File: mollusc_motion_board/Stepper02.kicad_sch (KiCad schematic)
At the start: 7 parts, among them J3 RJ45 x4, U6 74HC14, U6 SN74AHCT125N

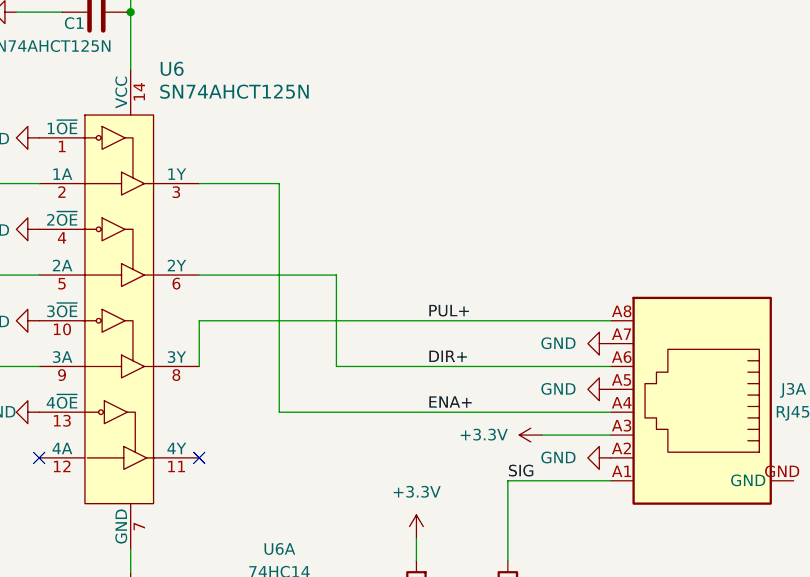
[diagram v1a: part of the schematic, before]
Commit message: adding ethernet jack
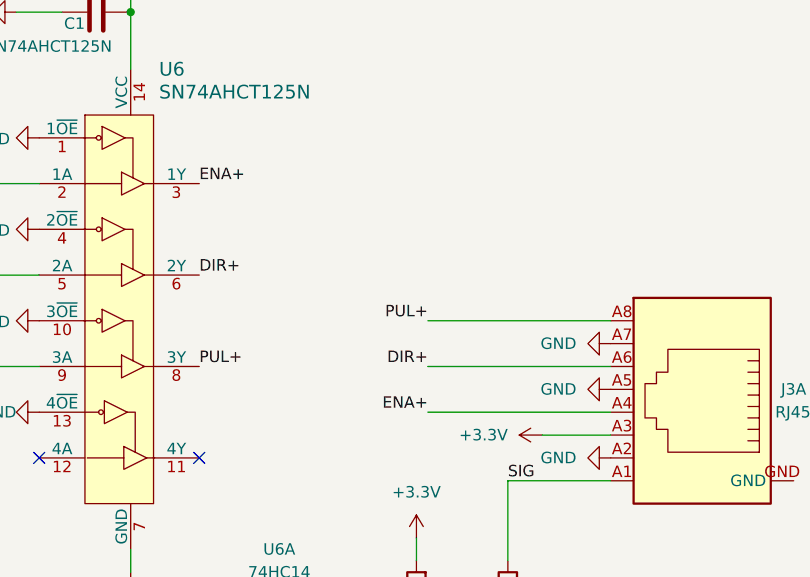
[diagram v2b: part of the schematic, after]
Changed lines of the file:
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@@
-    (stroke (width 0) (type default))
-  )
-  (wire (pts (xy 151.13 113.03) (xy 151.13 87.63))
     (stroke (width 0) (type default))
   )
@@
     (stroke (width 0) (type default))
   )
-  (wire (pts (xy 157.48 107.95) (xy 187.96 107.95))
-    (stroke (width 0) (type default))
-  )
-  (wire (pts (xy 142.24 102.87) (xy 142.24 107.95))
-    (stroke (width 0) (type default))
-  )
   (wire (pts (xy 176.53 120.65) (xy 187.96 120.65))
     (stroke (width 0) (type default))
   )
-  (wire (pts (xy 142.24 97.79) (xy 157.48 97.79))
+  (wire (pts (xy 167.64 113.03) (xy 187.96 113.03))
     (stroke (width 0) (type default))
   )
@@
     (stroke (width 0) (type default))
   )
-  (wire (pts (xy 157.48 97.79) (xy 157.48 107.95))
+  (wire (pts (xy 167.64 102.87) (xy 187.96 102.87))
     (stroke (width 0) (type default))
   )
@@
     (stroke (width 0) (type default))
   )
-  (wire (pts (xy 142.24 102.87) (xy 187.96 102.87))
-    (stroke (width 0) (type default))
-  )
   (wire (pts (xy 158.75 137.16) (xy 166.37 137.16))
     (stroke (width 0) (type default))
   )
-  (wire (pts (xy 134.62 128.27) (xy 134.62 130.81))
+  (wire (pts (xy 167.64 107.95) (xy 187.96 107.95))
     (stroke (width 0) (type default))
   )
-  (wire (pts (xy 151.13 113.03) (xy 187.96 113.03))
+  (wire (pts (xy 134.62 128.27) (xy 134.62 130.81))
     (stroke (width 0) (type default))
   )
@@
     (stroke (width 0) (type default))
   )
-  (wire (pts (xy 151.13 87.63) (xy 142.24 87.63))
-    (stroke (width 0) (type default))
-  )
   (wire (pts (xy 134.62 68.58) (xy 134.62 74.93))
     (stroke (width 0) (type default))
@@
     (effects (font (size 5.08 5.08)) (justify left bottom))
   )
-  (label "ENA+" (at 167.64 113.03 0) (fields_autoplaced)
+  (label "ENA+" (at 167.64 113.03 180) (fields_autoplaced)
+    (effects (font (size 1.27 1.27)) (justify right bottom))
+  )
+  (label "DIR+" (at 167.64 107.95 180) (fields_autoplaced)
+    (effects (font (size 1.27 1.27)) (justify right bottom))
+  )
+  (label "ENA+" (at 142.24 87.63 0) (fields_autoplaced)
     (effects (font (size 1.27 1.27)) (justify left bottom))
   )
-  (label "DIR+" (at 167.64 107.95 0) (fields_autoplaced)
+  (label "PUL+" (at 142.24 107.95 0) (fields_autoplaced)
     (effects (font (size 1.27 1.27)) (justify left bottom))
   )
@@
     (effects (font (size 1.27 1.27)) (justify left bottom))
   )
-  (label "PUL+" (at 167.64 102.87 0) (fields_autoplaced)
+  (label "DIR+" (at 142.24 97.79 0) (fields_autoplaced)
     (effects (font (size 1.27 1.27)) (justify left bottom))
   )
+  (label "PUL+" (at 167.64 102.87 180) (fields_autoplaced)
+    (effects (font (size 1.27 1.27)) (justify right bottom))
+  )
   (hierarchical_label "Stepper_ENABLE" (shape input) (at 114.3 87.63 180) (fields_autoplaced)

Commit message: Board v2 wip
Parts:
- C1, C3: value 0.1uF 16V -> 0.1uF 50V; footprint HangOn_Mainboard:R0603 -> molluscmotion:C0603
- R1, R2: footprint HangOn_Mainboard:R0603 -> molluscmotion:R0603
- U6: footprint HangOn_Mainboard:SOIC-14_L8.7-W3.9-P1.27-LS6.0-BL -> molluscmotion:SOIC-14_L8.7-W3.9-P1.27-LS6.0-BL
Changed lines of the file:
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@@
       (effects (font (size 1.27 1.27)) (justify left))
     )
-    (property "Value" "0.1uF 16V" (at 169.291 142.113 0)
-      (effects (font (size 1.27 1.27)) (justify left))
-    )
-    (property "Footprint" "HangOn_Mainboard:R0603" (at 167.3352 144.78 0)
+    (property "Value" "0.1uF 50V " (at 169.291 142.113 0)
+      (effects (font (size 1.27 1.27)) (justify left))
+    )
+    (property "Footprint" "molluscmotion:C0603" (at 167.3352 144.78 0)
       (effects (font (size 1.27 1.27)) hide)
     )
@@
       (effects (font (size 1.27 1.27)) (justify right))
     )
-    (property "Footprint" "HangOn_Mainboard:R0603" (at 168.148 133.35 90)
+    (property "Footprint" "molluscmotion:R0603" (at 168.148 133.35 90)
       (effects (font (size 1.27 1.27)) hide)
     )
@@
       (effects (font (size 1.27 1.27)))
     )
-    (property "Footprint" "HangOn_Mainboard:SOIC-14_L8.7-W3.9-P1.27-LS6.0-BL" (at 151.13 137.16 0)
+    (property "Footprint" "molluscmotion:SOIC-14_L8.7-W3.9-P1.27-LS6.0-BL" (at 151.13 137.16 0)
       (effects (font (size 1.27 1.27)) hide)
     )
@@
         )
         (path "/351cebb8-982f-46d7-8218-395788e5ce03/c416ce84-8678-4ab5-ab91-bfcc4d019431"
-          (reference "J4") (unit 2)
+          (reference "J4") (unit 3)
         )
       )
@@
       (effects (font (size 1.27 1.27)) (justify left))
     )
-    (property "Footprint" "HangOn_Mainboard:R0603" (at 174.752 133.35 90)
+    (property "Footprint" "molluscmotion:R0603" (at 174.752 133.35 90)
       (effects (font (size 1.27 1.27)) hide)
     )
@@
       (effects (font (size 1.524 1.524)) (justify left))
     )
-    (property "Footprint" "HangOn_Mainboard:SOIC-14_L8.7-W3.9-P1.27-LS6.0-BL" (at 139.7 87.63 0)
+    (property "Footprint" "molluscmotion:SOIC-14_L8.7-W3.9-P1.27-LS6.0-BL" (at 139.7 87.63 0)
       (effects (font (size 1.524 1.524)) (justify left) hide)
     )
@@
       (effects (font (size 1.27 1.27)) (justify left))
     )
-    (property "Value" "0.1uF 16V " (at 133.35 64.77 90)
-      (effects (font (size 1.27 1.27)) (justify left))
-    )
-    (property "Footprint" "HangOn_Mainboard:R0603" (at 134.62 67.6148 0)
-      (effects (font (size 1.27 1.27)) hide)
-    )
+    (property "Value" "0.1uF 50V " (at 133.35 64.77 90)
+      (effects (font (size 1.27 1.27)) (justify left))
+    )
+    (property "Footprint" "molluscmotion:C0603" (at 134.62 67.6148 0)
+      (effects (font (size 1.27 1.27)) hide)
+    )

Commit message: PCB v1.2 Layout
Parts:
- added D5: ESD5Z5_0T1G, molluscmotion:SOD-523F_L1.2-W0.8-LS1.7-RD, symbol molluscmotion:ESD5Z5_0T1G
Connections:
- net GND: now also D5.2 (A)
- net at C3.1, R1.1, R2.2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: now also D5.1 (C)
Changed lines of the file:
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@@
 (kicad_sch (version 20230121) (generator eeschema)
   (paper "A4")
+  (junction (at 171.45 148.59) (diameter 0) (color 0 0 0 0)
+  )
   (junction (at 166.37 137.16) (diameter 0) (color 0 0 0 0)
   )
   (junction (at 134.62 68.58) (diameter 0) (color 0 0 0 0)
+  )
+  (junction (at 176.53 137.16) (diameter 0) (color 0 0 0 0)
   )
   (no_connect (at 142.24 118.11))
@@
     (stroke (width 0) (type default))
   )
+  (wire (pts (xy 166.37 148.59) (xy 171.45 148.59))
+    (stroke (width 0) (type default))
+  )
+  (wire (pts (xy 176.53 147.32) (xy 176.53 148.59))
+    (stroke (width 0) (type default))
+  )
   (wire (pts (xy 114.3 97.79) (xy 124.46 97.79))
     (stroke (width 0) (type default))
@@
     (stroke (width 0) (type default))
   )
+  (wire (pts (xy 171.45 148.59) (xy 176.53 148.59))
+    (stroke (width 0) (type default))
+  )
   (wire (pts (xy 143.51 137.16) (xy 127 137.16))
     (stroke (width 0) (type default))
   )
-  (wire (pts (xy 166.37 147.32) (xy 166.37 144.78))
+  (wire (pts (xy 171.45 148.59) (xy 171.45 151.13))
     (stroke (width 0) (type default))
   )
   (wire (pts (xy 114.3 87.63) (xy 124.46 87.63))
+    (stroke (width 0) (type default))
+  )
+  (wire (pts (xy 166.37 144.78) (xy 166.37 148.59))
     (stroke (width 0) (type default))
   )
@@
   (symbol (lib_id "Device:C") (at 166.37 140.97 0) (unit 1)
     (in_bom yes) (on_board yes) (dnp no)
-    (property "Reference" "C3" (at 169.291 139.8016 0)
+    (property "Reference" "C3" (at 161.29 142.24 0)
       (effects (font (size 1.27 1.27)) (justify left))
     )
-    (property "Value" "0.1uF 50V " (at 169.291 142.113 0)
+    (property "Value" "0.1uF 50V " (at 160.02 144.78 0)
       (effects (font (size 1.27 1.27)) (justify left))
     )
@@
     )
   )
+  (symbol (lib_id "power:GND") (at 171.45 151.13 0) (unit 1)
+    (in_bom yes) (on_board yes) (dnp no)
+    (property "Reference" "#PWR07" (at 171.45 157.48 0)
+      (effects (font (size 1.27 1.27)) hide)
+    )
+    (property "Value" "GND" (at 173.99 154.94 0)
+      (effects (font (size 1.27 1.27)) (justify right))
+    )
+    (property "Footprint" "" (at 171.45 151.13 0)
+      (effects (font (size 1.27 1.27)) hide)
+    )
+    (property "Datasheet" "" (at 171.45 151.13 0)
+      (effects (font (size 1.27 1.27)) hide)
+    )
+    (pin "1")
+    (instances
+      (project "mollusc_motion_board"
+        (path "/351cebb8-982f-46d7-8218-395788e5ce03"
+          (reference "#PWR07") (unit 1)
+        )
+        (path "/351cebb8-982f-46d7-8218-395788e5ce03/679b5948-2929-4082-9ec3-0ebae5348a76"
+          (reference "#PWR07") (unit 1)
+        )
+        (path "/351cebb8-982f-46d7-8218-395788e5ce03/c416ce84-8678-4ab5-ab91-bfcc4d019431"
+          (reference "#PWR013") (unit 1)
+        )
+      )
+      (project "MechanicalTheatre"
+        (path "/7716aab8-fa4d-4c39-bbbe-a68aa4fb9c54/00000000-0000-0000-0000-00006111fd42"
+          (reference "#PWR063") (unit 1)
+        )
+      )
+    )
+  )
   (symbol (lib_id "power:GND") (at 124.46 82.55 270) (unit 1)
     (in_bom yes) (on_board yes) (dnp no)
@@
     )
   )
-  (symbol (lib_id "power:GND") (at 166.37 147.32 0) (unit 1)
-    (in_bom yes) (on_board yes) (dnp no)
-    (property "Reference" "#PWR07" (at 166.37 153.67 0)
-      (effects (font (size 1.27 1.27)) hide)
-    )
-    (property "Value" "GND" (at 165.1 148.59 0)
-      (effects (font (size 1.27 1.27)) (justify right))
-    )
-    (property "Footprint" "" (at 166.37 147.32 0)
-      (effects (font (size 1.27 1.27)) hide)
-    )
-    (property "Datasheet" "" (at 166.37 147.32 0)
-      (effects (font (size 1.27 1.27)) hide)
-    )
-    (pin "1")
-    (instances
-      (project "mollusc_motion_board"
-        (path "/351cebb8-982f-46d7-8218-395788e5ce03"
-          (reference "#PWR07") (unit 1)
-        )
-        (path "/351cebb8-982f-46d7-8218-395788e5ce03/679b5948-2929-4082-9ec3-0ebae5348a76"
-          (reference "#PWR07") (unit 1)
-        )
-        (path "/351cebb8-982f-46d7-8218-395788e5ce03/c416ce84-8678-4ab5-ab91-bfcc4d019431"
-          (reference "#PWR020") (unit 1)
-        )
-      )
-      (project "MechanicalTheatre"
-        (path "/7716aab8-fa4d-4c39-bbbe-a68aa4fb9c54/00000000-0000-0000-0000-00006111fd42"
-          (reference "#PWR063") (unit 1)
-        )
-      )
+  (symbol (lib_id "molluscmotion:ESD5Z5_0T1G") (at 176.53 142.24 270) (unit 1)
+    (in_bom yes) (on_board yes) (dnp no)
+    (property "Reference" "D5" (at 180.34 142.24 90)
+      (effects (font (size 1.27 1.27)))
+    )
+    (property "Value" "ESD5Z5_0T1G" (at 184.15 144.78 90)
+      (effects (font (size 1.27 1.27)))
+    )
+    (property "Footprint" "molluscmotion:SOD-523F_L1.2-W0.8-LS1.7-RD" (at 166.37 142.24 0)
+      (effects (font (size 1.27 1.27) italic) hide)
+    )
+    (property "Datasheet" "https://item.szlcsc.com/235389.html" (at 176.657 139.954 0)
+      (effects (font (size 1.27 1.27)) (justify left) hide)
+    )
+    (property "LCSC" "C82044" (at 176.53 142.24 0)
+      (effects (font (size 1.27 1.27)) hide)
+    )
+    (pin "1")
+    (pin "2")
+    (instances
+      (project "mollusc_motion_board"
+        (path "/351cebb8-982f-46d7-8218-395788e5ce03/679b5948-2929-4082-9ec3-0ebae5348a76"
+          (reference "D5") (unit 1)
+        )
+        (path "/351cebb8-982f-46d7-8218-395788e5ce03/c416ce84-8678-4ab5-ab91-bfcc4d019431"
+          (reference "D4") (unit 1)
+        )
+      )
